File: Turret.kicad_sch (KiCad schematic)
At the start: 29 parts

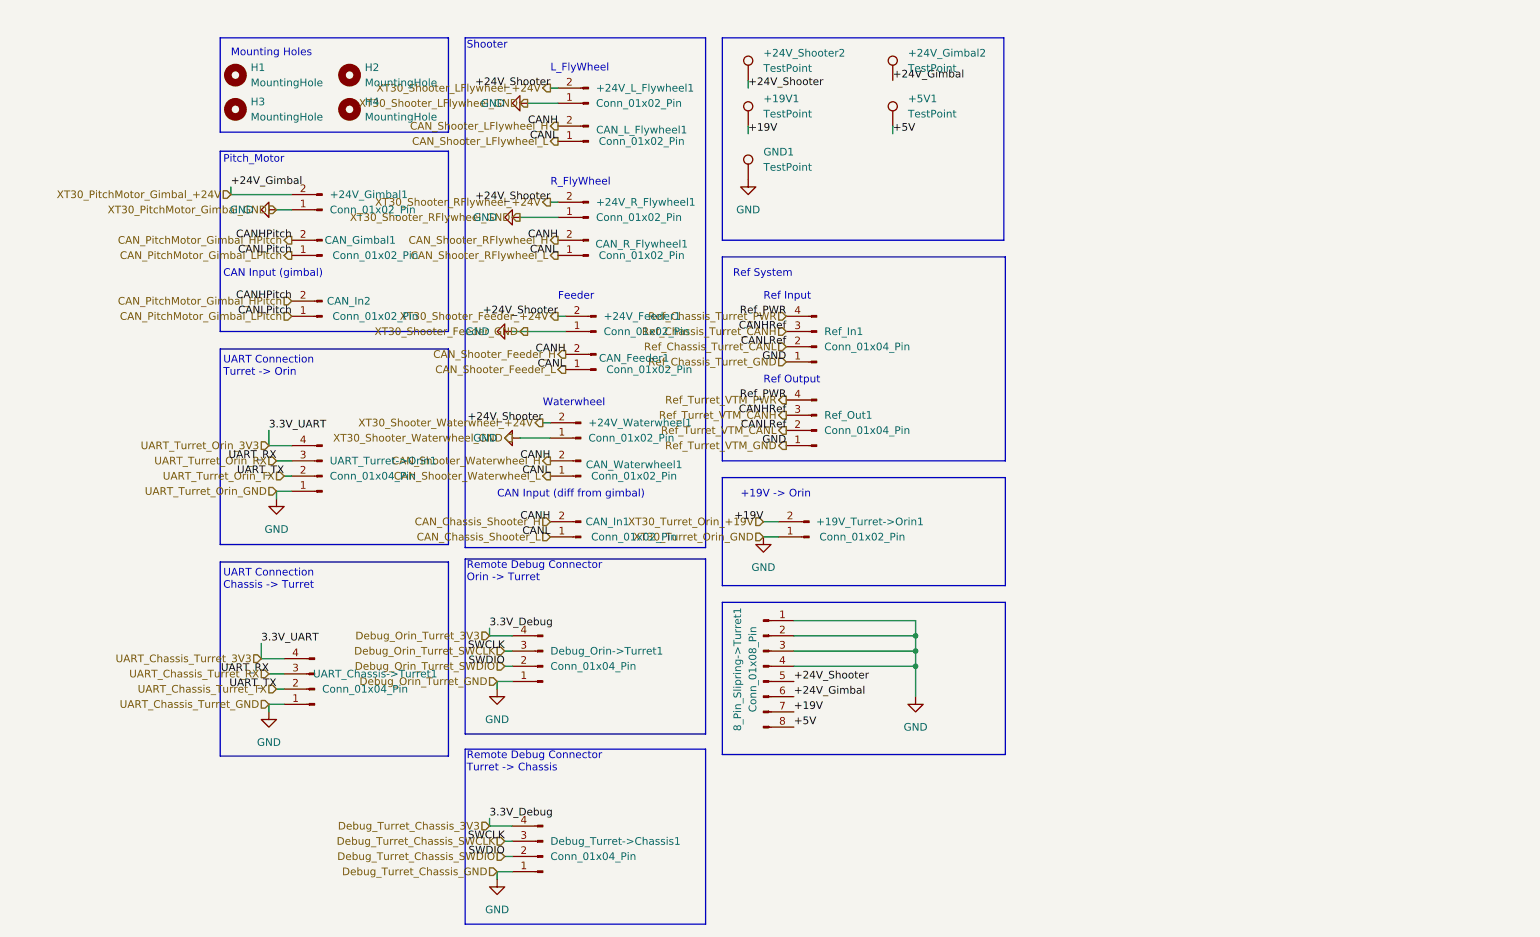
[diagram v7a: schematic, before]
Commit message: Cleaned up hierarchical labels
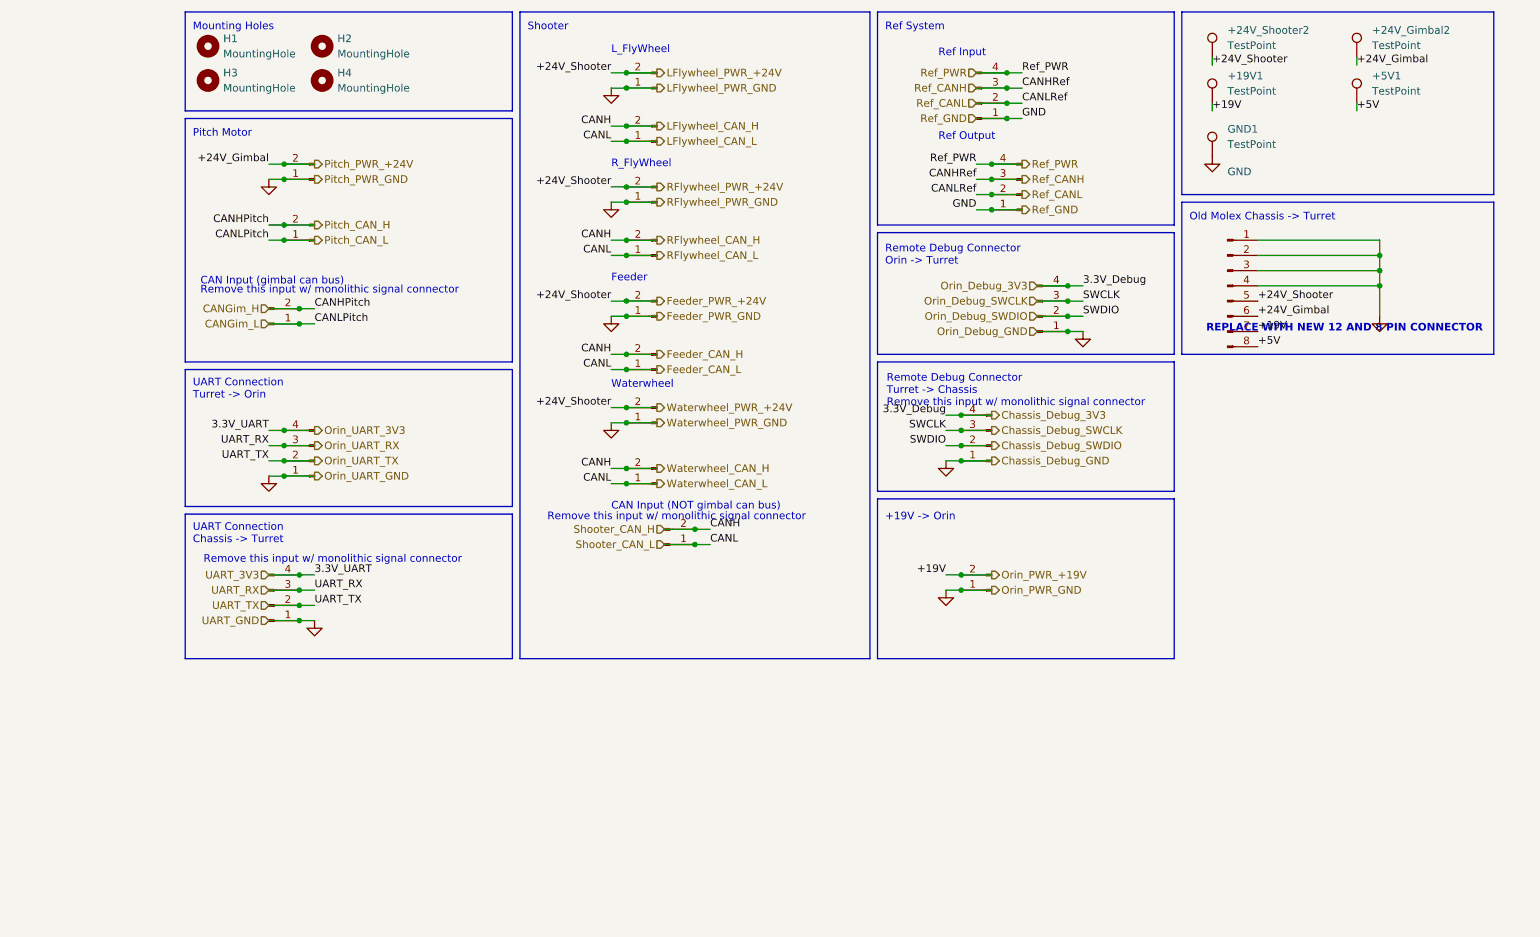
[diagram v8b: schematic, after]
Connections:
- net CAN_Chassis_Shooter_H renamed Feeder_CAN_H
- net CAN_Chassis_Shooter_L renamed Feeder_CAN_L
- net CAN_PitchMotor_Gimbal_HPitch renamed CANGim_H
- net CAN_PitchMotor_Gimbal_LPitch renamed CANGim_L
- net Debug_Orin_Turret_3V3 renamed Chassis_Debug_3V3
- net Debug_Orin_Turret_SWCLK renamed Chassis_Debug_SWCLK
- net Debug_Orin_Turret_SWDIO renamed Chassis_Debug_SWDIO
- net Ref_Chassis_Turret_CANH renamed Ref_CANH
- net Ref_Chassis_Turret_CANL renamed Ref_CANL
- net Ref_Chassis_Turret_PWR renamed Ref_PWR
- net UART_Chassis_Turret_3V3 renamed Orin_UART_3V3
- net UART_Chassis_Turret_RX renamed Orin_UART_RX
- net UART_Chassis_Turret_TX renamed Orin_UART_TX
- net XT30_PitchMotor_Gimbal_+24V renamed Pitch_PWR_+24V
- net XT30_Shooter_Feeder_+24V renamed Feeder_PWR_+24V
- net XT30_Turret_Orin_+19V renamed Orin_PWR_+19V
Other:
- note added: "CAN Input (NOT gimbal can bus)"
- note added: "CAN Input (gimbal can bus)"
- note added: "Old Molex Chassis -> Turret"
- note added: "Pitch Motor"
- note added: "REPLACE WITH NEW 12 AND 8 PIN CONNECTOR"
- note added: "Remove this input w/ monolithic signal connector"
- note removed: "CAN Input (diff from gimbal)"
- note removed: "CAN Input (gimbal)"
- note removed: "Pitch_Motor"
- moved on the sheet: +19V1, +24V_Gimbal2, +24V_Shooter2, +5V1, GND1, H1, H2, H3, H4
